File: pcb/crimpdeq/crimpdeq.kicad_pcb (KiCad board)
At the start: 2 copper layers, 23 x 63.8 mm, 49 parts, among them J2 USB4105-GF-A, J3 Loadcell_Pads, J4 Sense_Pads, J5 Battery_Switch_Pads, Q1 SS8550, Q2 DMG3415U, U1 ESP32-C3-MINI-1, U2 MCP73831T-2ACI/OT, U3 HX711, U5 MAX17048G+T10, U6 SY8088

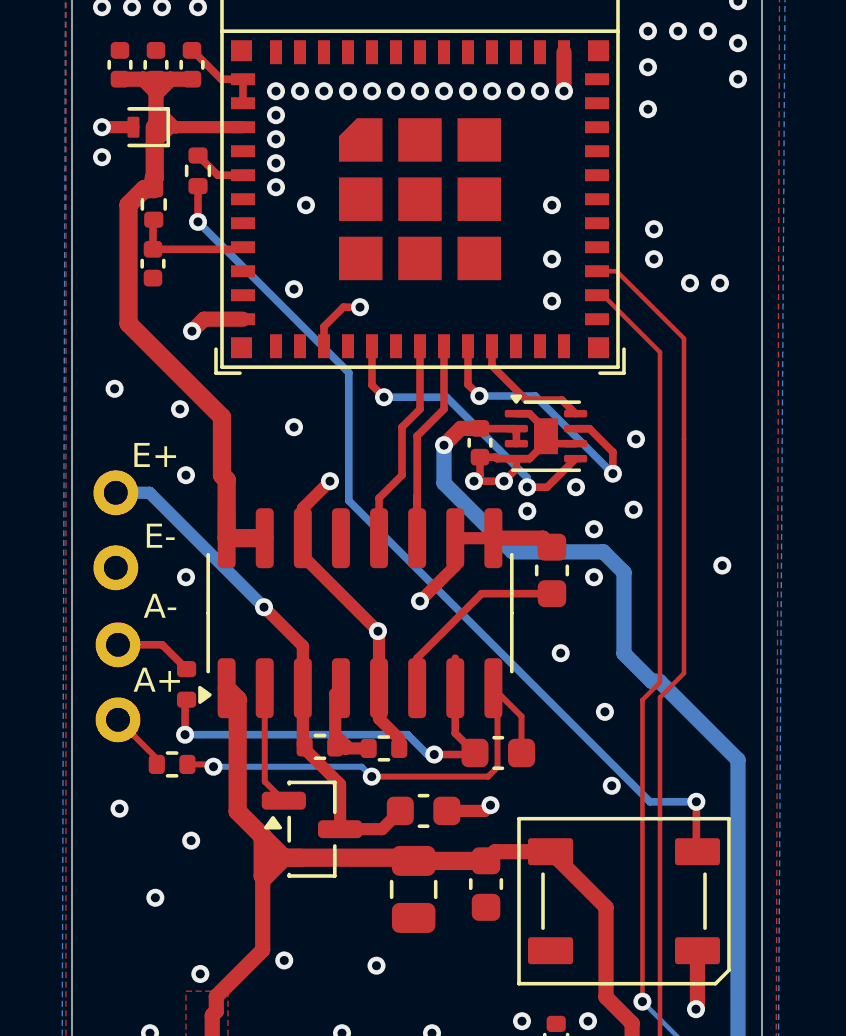
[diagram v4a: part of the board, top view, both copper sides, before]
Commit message: feat: link external pads to schematic
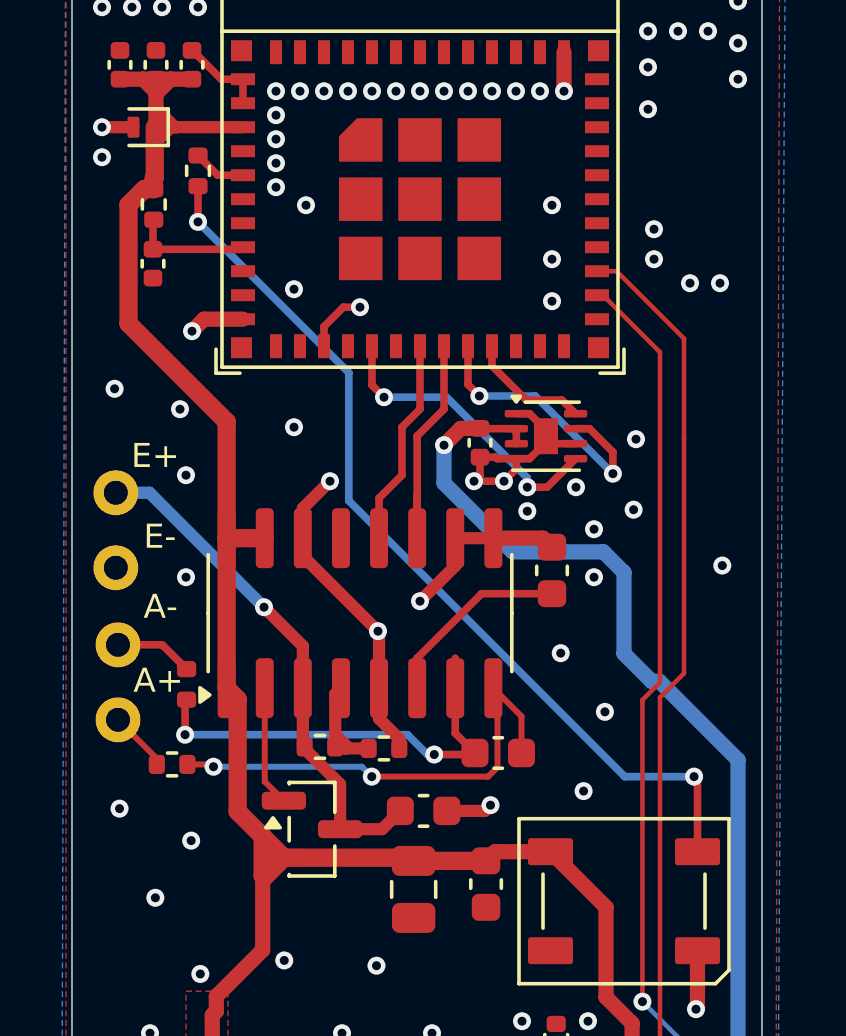
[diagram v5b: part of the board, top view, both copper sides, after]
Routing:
- net +3V3: track 65.0 -> 70.0 mm
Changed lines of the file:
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@@
 			)
 		)
-		(attr through_hole board_only)
+		(sheetname "/")
+		(sheetfile "crimpdeq.kicad_sch")
+		(attr through_hole)
 		(duplicate_pad_numbers_are_jumpers no)
 		(fp_text user "A+"
@@
 			)
 		)
-		(attr through_hole board_only)
+		(sheetname "/")
+		(sheetfile "crimpdeq.kicad_sch")
+		(attr through_hole)
 		(duplicate_pad_numbers_are_jumpers no)
 		(fp_text user "E+"
@@
 			)
 		)
-		(attr through_hole board_only)
+		(sheetname "/")
+		(sheetfile "crimpdeq.kicad_sch")
+		(attr through_hole)
 		(duplicate_pad_numbers_are_jumpers no)
 		(fp_text user "B+"
@@
 	)
 	(via
-		(at 147.193 77.9526)
+		(at 146.2532 78.1304)
 		(size 0.6)
 		(drill 0.3)
@@
 	)
 	(segment
-		(start 134.2 67.6)
-		(end 134.2 65.66184)
+		(start 134.355 74.7)
+		(end 134.355 69.7)
 		(width 0.6096)
 		(layer "F.Cu")
@@
 	)
 	(segment
+		(start 131.925 58.065)
+		(end 131.605001 58.065)
+		(width 0.6096)
+		(layer "F.Cu")
+		(net "+3V3")
+	)
+	(segment
 		(start 132 55.95)
 		(end 131.95 56)
@@
 	)
 	(segment
-		(start 131.0852 62.54704)
-		(end 131.0852 58.584801)
-		(width 0.6096)
-		(layer "F.Cu")
-		(net "+3V3")
-	)
-	(segment
 		(start 143.3062 80.15)
 		(end 143.002 80.4542)
@@
 	)
 	(segment
+		(start 131.605001 58.065)
+		(end 131.0852 58.584801)
+		(width 0.6096)
+		(layer "F.Cu")
+		(net "+3V3")
+	)
+	(segment
 		(start 132.6896 56)
 		(end 132.5 56)
@@
 	)
 	(segment
-		(start 134.355 69.7)
-		(end 134.355 67.755)
-		(width 0.6096)
-		(layer "F.Cu")
-		(net "+3V3")
-	)
-	(segment
 		(start 134.9 56)
 		(end 132.6896 56)
@@
 	)
 	(segment
-		(start 131.0852 58.584801)
-		(end 131.605001 58.065)
-		(width 0.6096)
-		(layer "F.Cu")
-		(net "+3V3")
-	)
-	(segment
-		(start 131.605001 58.065)
-		(end 131.925 58.065)
-		(width 0.6096)
-		(layer "F.Cu")
-		(net "+3V3")
-	)
-	(segment
 		(start 133.875 85.6064)
 		(end 134.0104 85.471)
@@
 	)
 	(segment
-		(start 134.2 65.66184)
-		(end 131.0852 62.54704)
-		(width 0.6096)
-		(layer "F.Cu")
-		(net "+3V3")
-	)
-	(segment
 		(start 133.65 90.575)
 		(end 133.875 90.8)
@@
 	)
 	(segment
+		(start 131.0852 62.54704)
+		(end 134.355 65.81684)
+		(width 0.6096)
+		(layer "F.Cu")
+		(net "+3V3")
+	)
+	(segment
 		(start 131.958 57.6784)
 		(end 131.958 56)
@@
 	)
 	(segment
+		(start 134.355 69.7)
+		(end 135.625 69.7)
+		(width 0.6096)
+		(layer "F.Cu")
+		(net "+3V3")
+	)
+	(segment
 		(start 132 54.864)
 		(end 132.0224 54.864)
@@
 	)
 	(segment
+		(start 134.355 65.81684)
+		(end 134.355 69.7)
+		(width 0.6096)
+		(layer "F.Cu")
+		(net "+3V3")
+	)
+	(segment
 		(start 132.0224 54.864)
 		(end 132.0224 54.8504)
@@
 	)
 	(segment
-		(start 134.0104 84.973282)
-		(end 135.55625 83.427432)
-		(width 0.508)
+		(start 131.0852 58.584801)
+		(end 131.0852 62.54704)
+		(width 0.6096)
 		(layer "F.Cu")
 		(net "+3V3")
 	)
 	(segment
-		(start 134.355 69.7)
-		(end 135.625 69.7)
-		(width 0.6096)
+		(start 134.0104 84.973282)
+		(end 135.55625 83.427432)
+		(width 0.508)
 		(layer "F.Cu")
 		(net "+3V3")
@@
 	)
 	(segment
-		(start 134.355 67.755)
-		(end 134.2 67.6)
-		(width 0.6096)
-		(layer "F.Cu")
-		(net "+3V3")
-	)
-	(segment
 		(start 136.2625 80.35)
 		(end 140.482 80.35)
@@
 	)
 	(segment
-		(start 150.0124 78.486)
-		(end 150.0124 80.1124)
+		(start 150.05 80.15)
+		(end 150.05 77.7616)
 		(width 0.254)
 		(layer "F.Cu")
@@
 		(net "Net-(D4-DIN)")
 	)
+	(segment
+		(start 150.05 77.7616)
+		(end 149.9362 77.6478)
+		(width 0.254)
+		(layer "F.Cu")
+		(net "Net-(D4-DIN)")
+	)
 	(via
-		(at 133.4008 59.1566)
+		(at 149.9362 77.6478)
 		(size 0.6)
 		(drill 0.3)
@@
 	)
 	(via
-		(at 150.0124 78.486)
+		(at 133.4008 59.1566)
 		(size 0.6)
 		(drill 0.3)
@@
 	)
 	(segment
-		(start 138.427 68.45)
-		(end 148.463 78.486)
+		(start 147.6248 77.6478)
+		(end 138.427 68.45)
 		(width 0.254)
 		(layer "B.Cu")
@@
 	)
 	(segment
-		(start 148.463 78.486)
-		(end 150.0124 78.486)
+		(start 149.9362 77.6478)
+		(end 147.6248 77.6478)
 		(width 0.254)
 		(layer "B.Cu")
